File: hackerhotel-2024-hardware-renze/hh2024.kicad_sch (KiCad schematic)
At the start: 56 parts, among them J1 SAO_connector, J3 Micro_SD_Card, J4 USB-C, SW1 Multi-Directional-Switches, SW2 Multi-Directional-Switches, SW3 Multi-Directional-Switches, SW4 Multi-Directional-Switches, SW5 Multi-Directional-Switches, U5 CH32V003F4U6

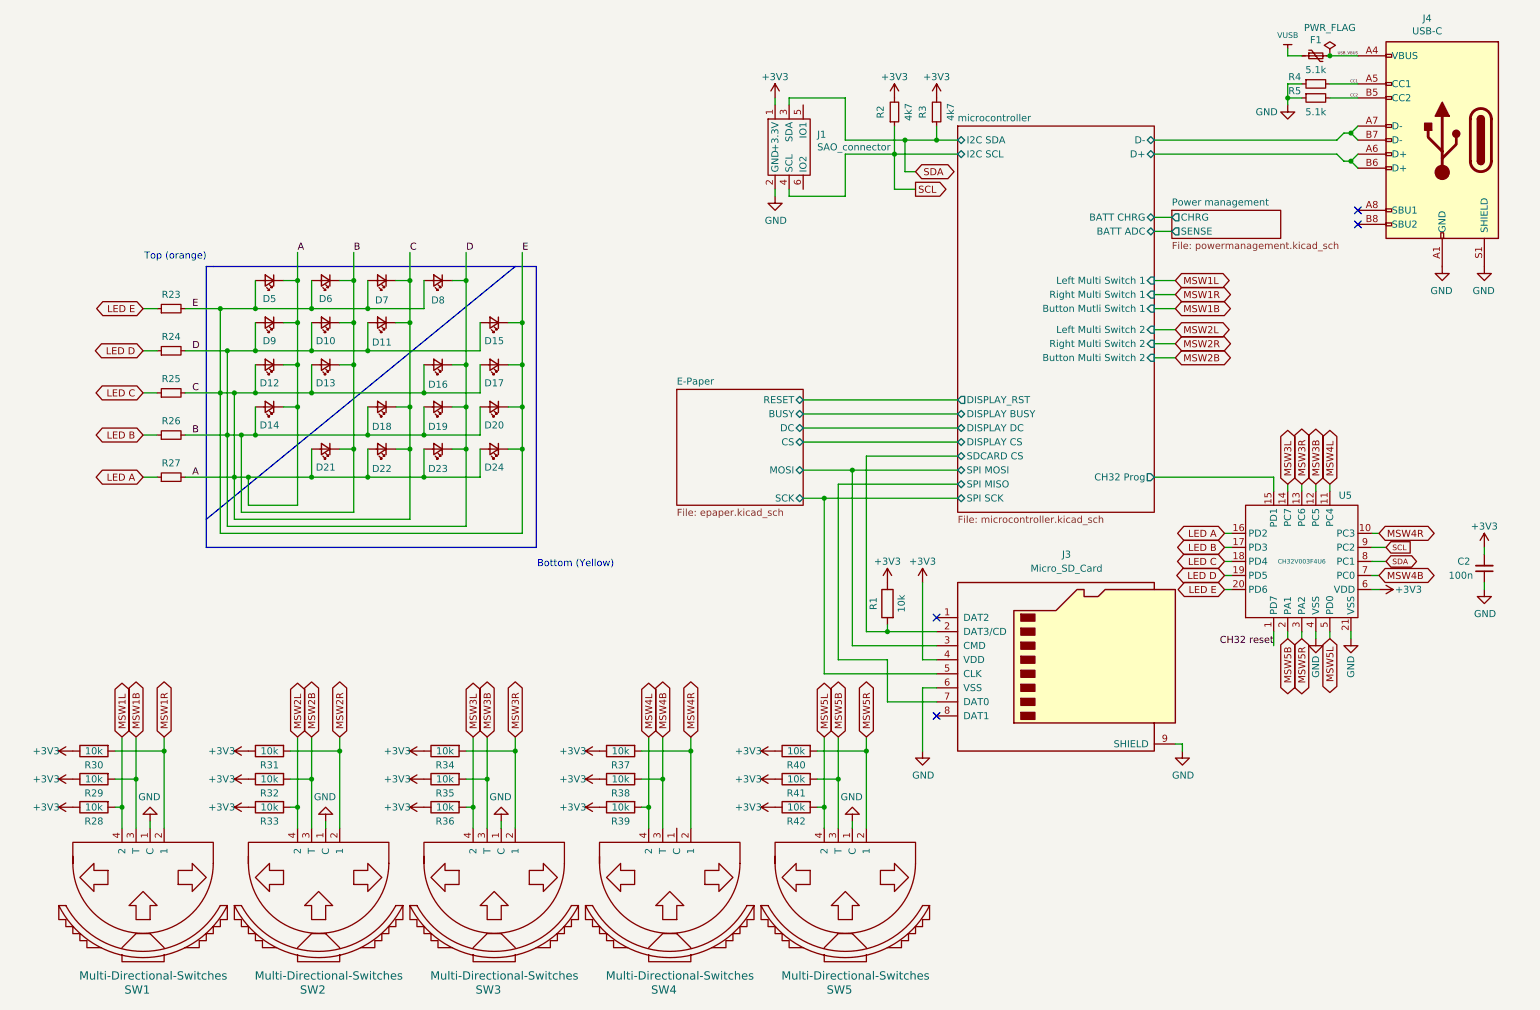
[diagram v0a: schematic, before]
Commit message: V1.1 schematic
Added a relay for clicking noise
Multiplexed the switches and moved them all to the CH32
Wired an ESP32 low power triggered pin (GPIO4) to PC4 on the CH32 so it can wake it up on input change
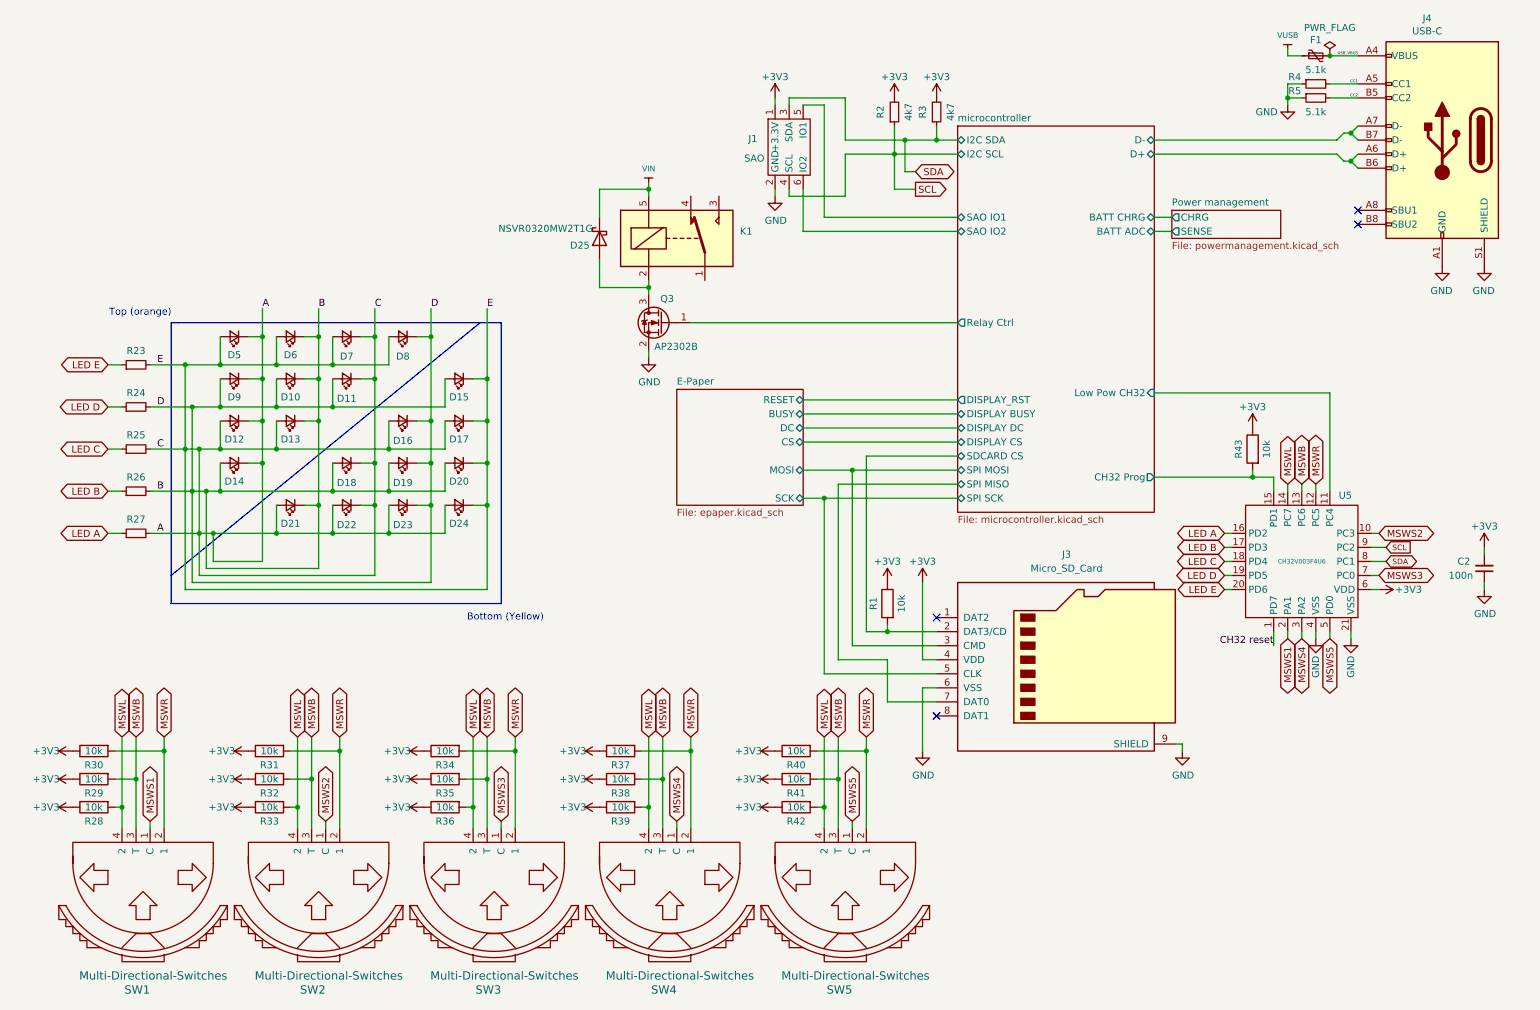
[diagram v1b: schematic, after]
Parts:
- added D25: NSVR0320MW2T1G, tanoshii:D_SOD-323, symbol symbols:D_Schottky
- added K1: SANYOU_SRD_Form_C, BamboulabFootprints:HRS1H-S-DC3V, symbol Relay:SANYOU_SRD_Form_C
- added Q3: AP2302B, tanoshii:SOT-23, symbol symbols:Q_NMOS_GSD
- added R43: 10k, Resistor_SMD:R_0805_2012Metric, symbol symbols:R
- J1: value SAO_connector -> SAO
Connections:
- net MSW2B is gone; now on net MSWB: R32.2, SW2.3 (T)
- net MSW2L is gone; now on net MSWL: R33.2, SW2.4 (2)
- net MSW2R is gone; now on net MSWR: R31.2, SW2.2 (1)
- net MSW3L is gone; now on net MSWL: R36.2, SW3.4 (2), U5.14 (PC7)
- net +3V3: now also R43.1
- net GND: now also Q3.2 (S); no longer SW1.1 (C), SW2.1 (C), SW3.1 (C), SW5.1 (C)
- net microcontroller/CH32 Prog: now also R43.2
- net microcontroller/SAO IO1: now reaches J1.5 (IO1)
- net microcontroller/SAO IO2: now reaches J1.6 (IO2)
- net MSWS4: now reaches SW4.1 (C)
- net MSWS4: now also U5.3 (PA2)
- net MSW1B renamed MSWB
- net MSWB: now also R35.2, R38.2, R41.2, SW3.3 (T), SW4.3 (T), SW5.3 (T), U5.13 (PC6)
- net MSW1L renamed MSWL
- net MSWL: now also R39.2, R42.2, SW4.4 (2), SW5.4 (2)
- net MSW1R renamed MSWR
- net MSWR: now also R34.2, R37.2, R40.2, SW3.2 (1), SW4.2 (1), SW5.2 (1), U5.12 (PC5)
- removed net MSW3B: R35.2, SW3.3 (T), U5.12 (PC5)
- removed net MSW3R: R34.2, SW3.2 (1), U5.13 (PC6)
- removed net MSW4B: R38.2, SW4.3 (T), U5.7 (PC0)
- removed net MSW4L: R39.2, SW4.4 (2), U5.11 (PC4)
- removed net MSW4R: R37.2, SW4.2 (1), U5.10 (PC3)
- removed net MSW5B: R41.2, SW5.3 (T), U5.2 (PA1)
- removed net MSW5L: R42.2, SW5.4 (2), U5.5 (PD0)
- removed net MSW5R: R40.2, SW5.2 (1), U5.3 (PA2)
- new net: D25.2 (A), K1.2, Q3.3 (D)
- new net MSWS1: SW1.1 (C), U5.2 (PA1)
- new net MSWS2: SW2.1 (C), U5.10 (PC3)
- new net MSWS3: SW3.1 (C), U5.7 (PC0)
- new net MSWS5: SW5.1 (C), U5.5 (PD0)
- new net VIN: D25.1 (K), K1.5
- new net microcontroller/Low Pow CH32: U5.11 (PC4)
- new net microcontroller/Relay Ctrl: Q3.1 (G)
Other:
- sheet microcontroller ports: added Low Pow CH32, Relay Ctrl, SAO IO1, SAO IO2; removed Button Multi Switch 2, Button Mutli Switch 1, Left Multi Switch 1, Left Multi Switch 2, Right Multi Switch 1, Right Multi Switch 2
- moved on the sheet: D10, D11, D12, D13, D14, D15, D16, D17, D18, D19, D20, D21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

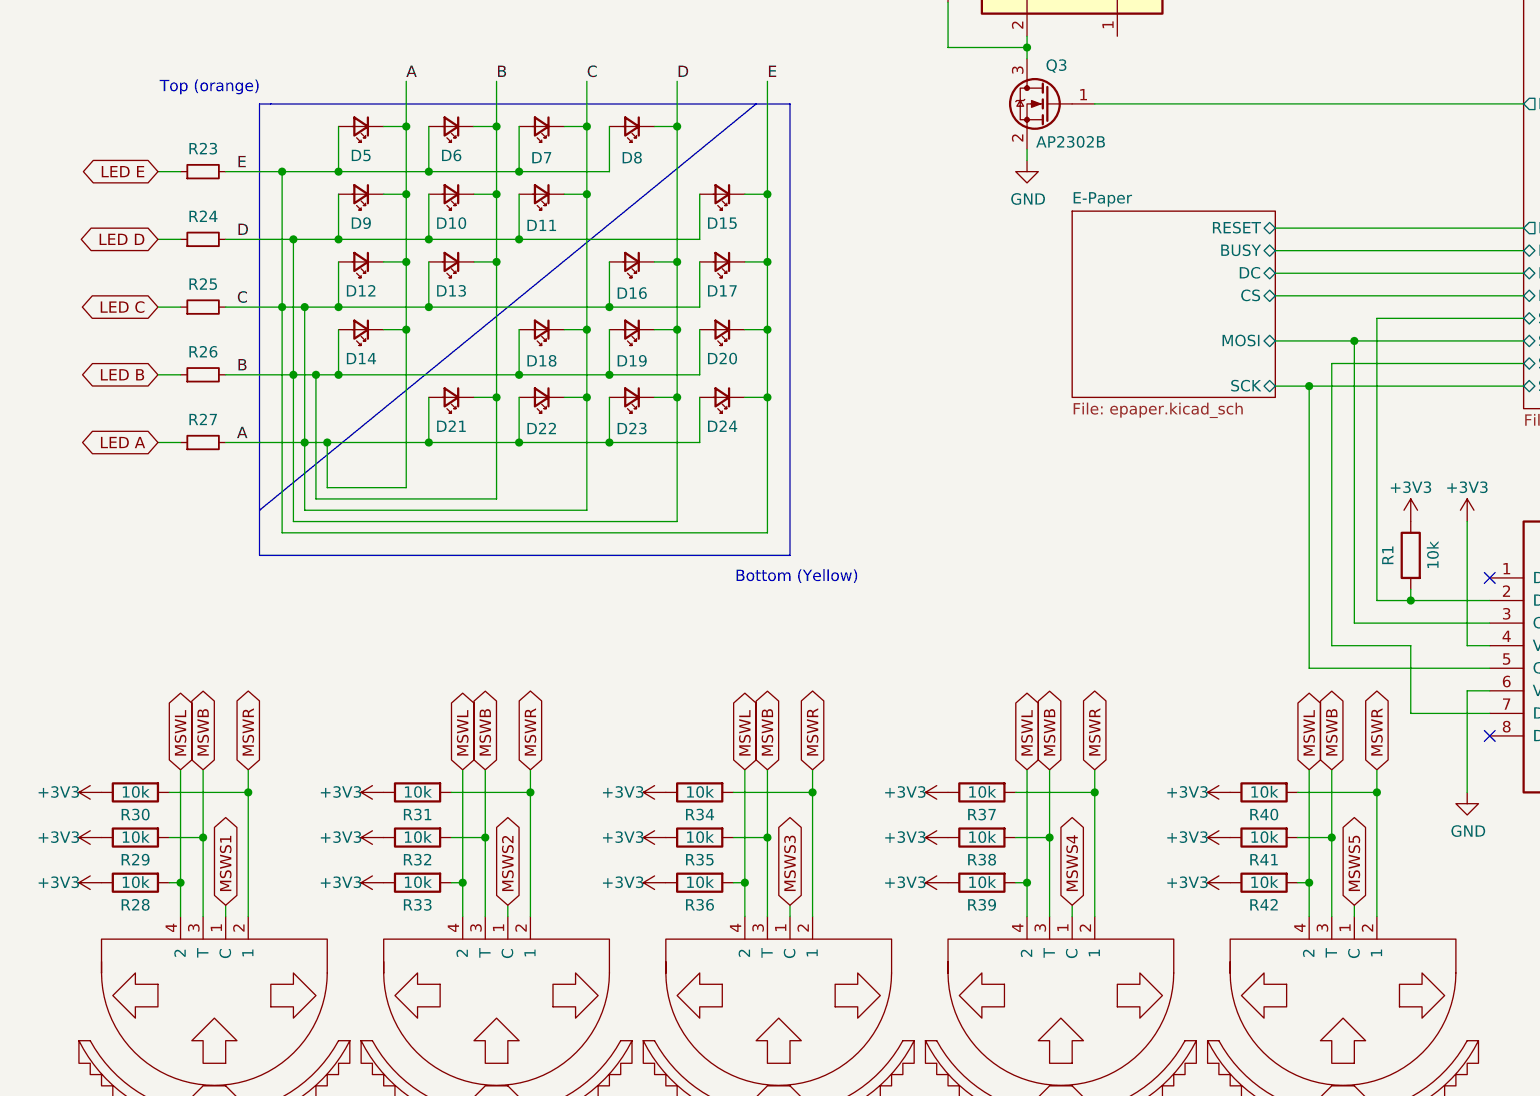
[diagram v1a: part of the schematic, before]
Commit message: Started layout
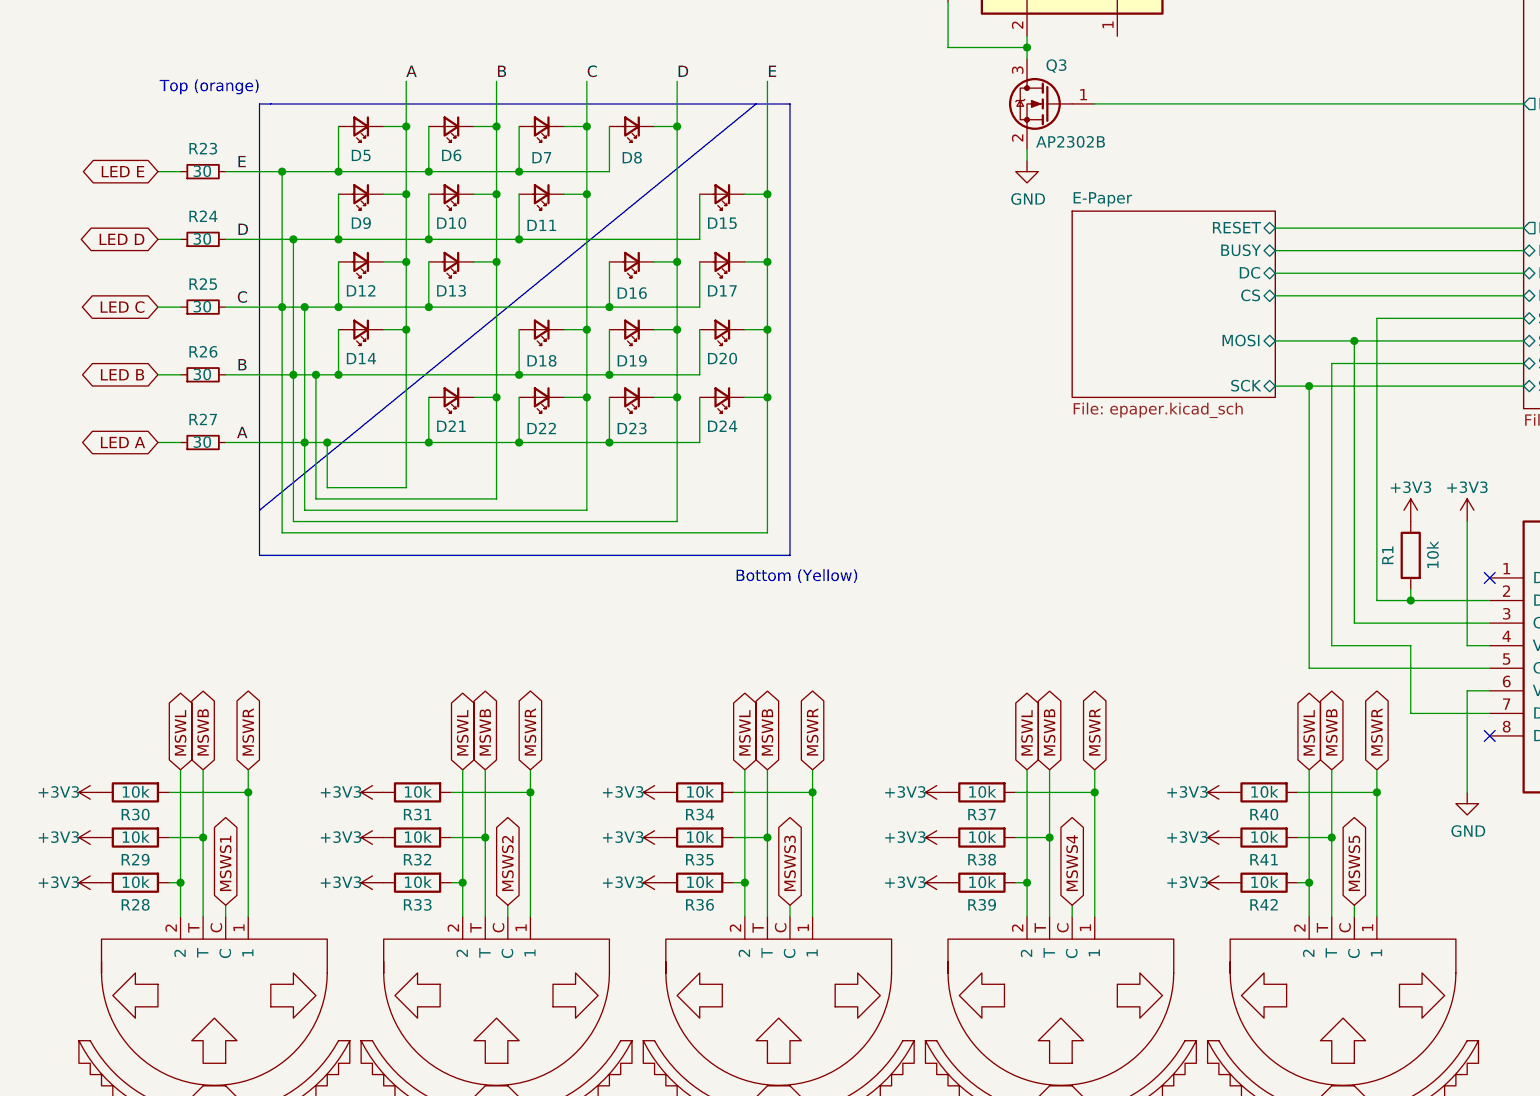
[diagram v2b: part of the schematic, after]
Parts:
- R23, R24, R25, R26, R27: value R_Small -> 30
- SW1, SW2, SW3, SW4, SW5: symbol eggWatch-rescue:Multi-Directional-Switches-bambouLab-eggWatch-rescue-eggWatch-rescue -> bambouLab:Multi_Directional_Switches_TM-2023
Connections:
- net MSWB: now also SW1.T, SW2.T, SW3.T, SW4.T, SW5.T; no longer SW1.3 (T), SW2.3 (T), SW3.3 (T), SW4.3 (T), SW5.3 (T)
- net MSWL: now also SW1.2, SW2.2, SW3.2, SW4.2, SW5.2; no longer SW1.4 (2), SW2.4 (2), SW3.4 (2), SW4.4 (2), SW5.4 (2)
- net MSWR: now also SW1.1, SW2.1, SW3.1, SW4.1, SW5.1; no longer SW1.2 (1), SW2.2 (1), SW3.2 (1), SW4.2 (1), SW5.2 (1)
- net MSWS1: now also SW1.C; no longer SW1.1 (C)
- net MSWS2: now also SW2.C; no longer SW2.1 (C)
- net MSWS3: now also SW3.C; no longer SW3.1 (C)
- net MSWS4: now also SW4.C; no longer SW4.1 (C)
- net MSWS5: now also SW5.C; no longer SW5.1 (C)

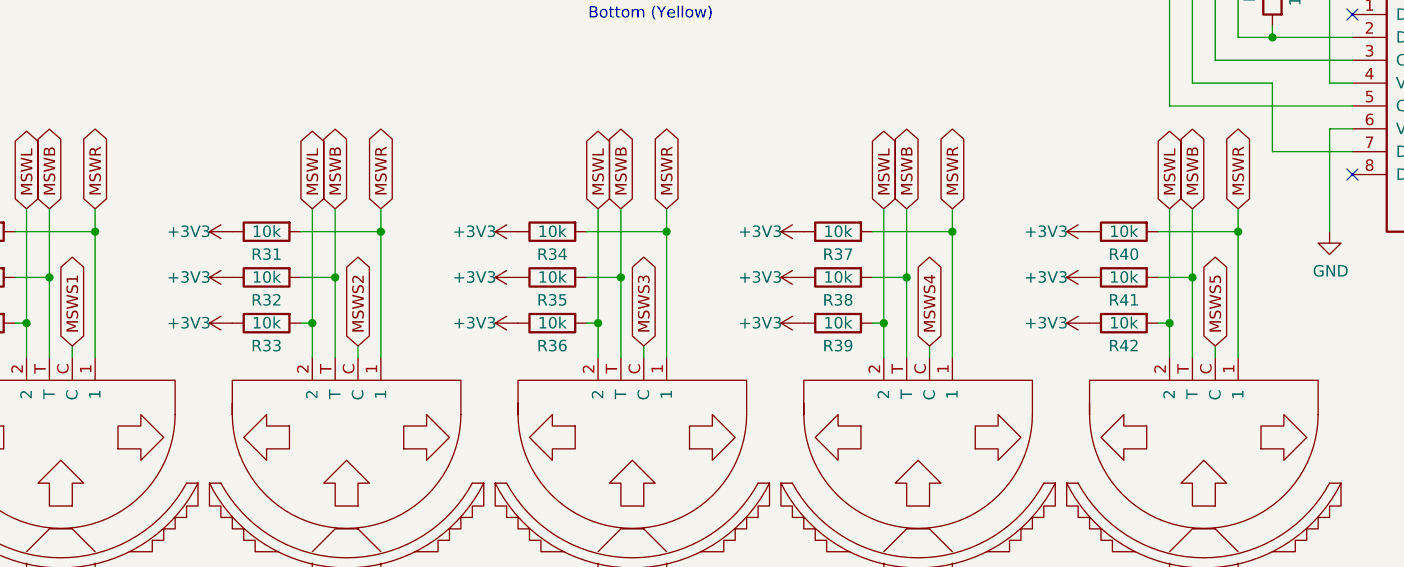
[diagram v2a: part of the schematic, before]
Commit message: removed extra pull ups on multi switches
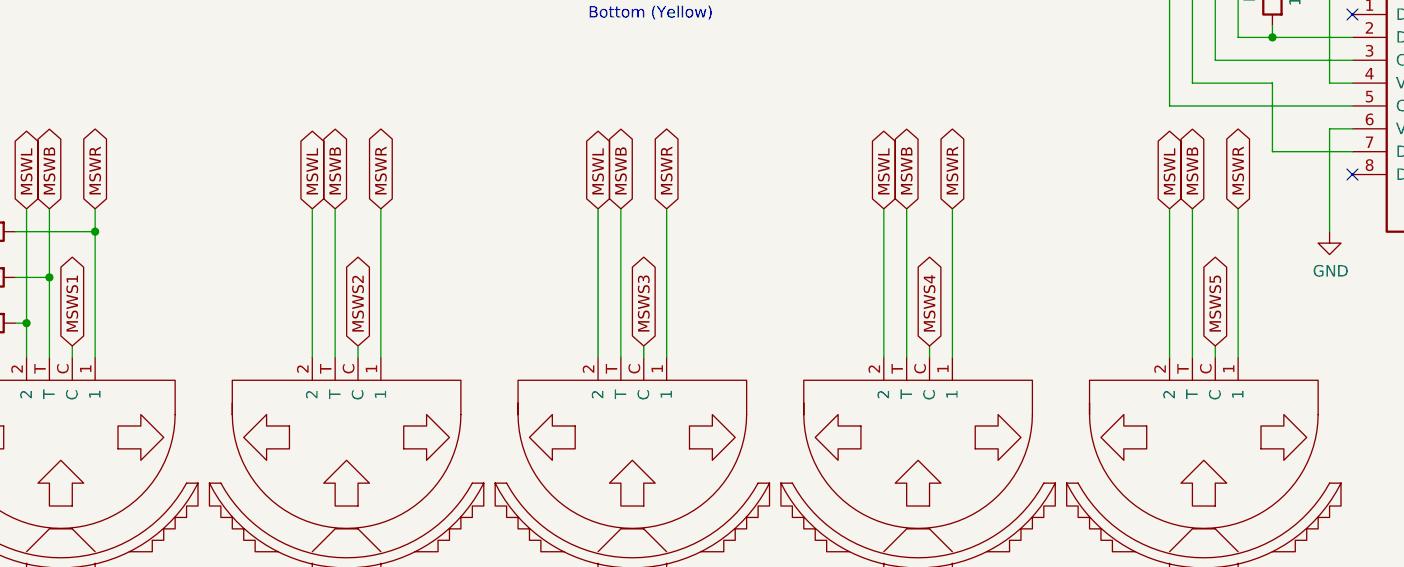
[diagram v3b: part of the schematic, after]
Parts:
- removed R31, R32, R33, R34, R35, R36, R37, R38, R39, R40, R41, R42: 10k, Resistor_SMD:R_0805_2012Metric, symbol symbols:R
